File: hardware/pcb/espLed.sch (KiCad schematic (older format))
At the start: 23 parts, among them J1 led_strip, J2 flashing, J3 power, Q1 IRF9310TRPBF, Q2 AO3400A, Q3 AO3400A, Q4 AO3400A, SW1 reset, SW2 flash, U1 AMS1117-3.3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

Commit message: fix default SOT23 footprint for AO3400 mosfet
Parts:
- Q2, Q3, Q4: footprint Package_TO_SOT_SMD:SOT-23 -> custom:AO3400
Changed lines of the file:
@@
 F 0 "Q2" V 2450 4650 50  0000 L CNN
 F 1 "AO3400A" V 2375 4425 50  0000 L CNN
-F 2 "Package_TO_SOT_SMD:SOT-23" H 2375 4950 50  0001 C CNN
+F 2 "custom:AO3400" H 2375 4950 50  0001 C CNN
 F 3 "https://static.chipdip.ru/lib/046/DOC003046153.pdf" H 2175 4850 50  0001 C CNN
 	1    2175 4850
@@
 F 0 "Q3" V 3550 4650 50  0000 L CNN
 F 1 "AO3400A" V 3475 4425 50  0000 L CNN
-F 2 "Package_TO_SOT_SMD:SOT-23" H 3475 4950 50  0001 C CNN
+F 2 "custom:AO3400" H 3475 4950 50  0001 C CNN
 F 3 "https://static.chipdip.ru/lib/046/DOC003046153.pdf" H 3275 4850 50  0001 C CNN
 	1    3275 4850
@@
 F 0 "Q4" V 4650 4650 50  0000 L CNN
 F 1 "AO3400A" V 4575 4425 50  0000 L CNN
-F 2 "Package_TO_SOT_SMD:SOT-23" H 4575 4950 50  0001 C CNN
+F 2 "custom:AO3400" H 4575 4950 50  0001 C CNN
 F 3 "https://static.chipdip.ru/lib/046/DOC003046153.pdf" H 4375 4850 50  0001 C CNN
 	1    4375 4850

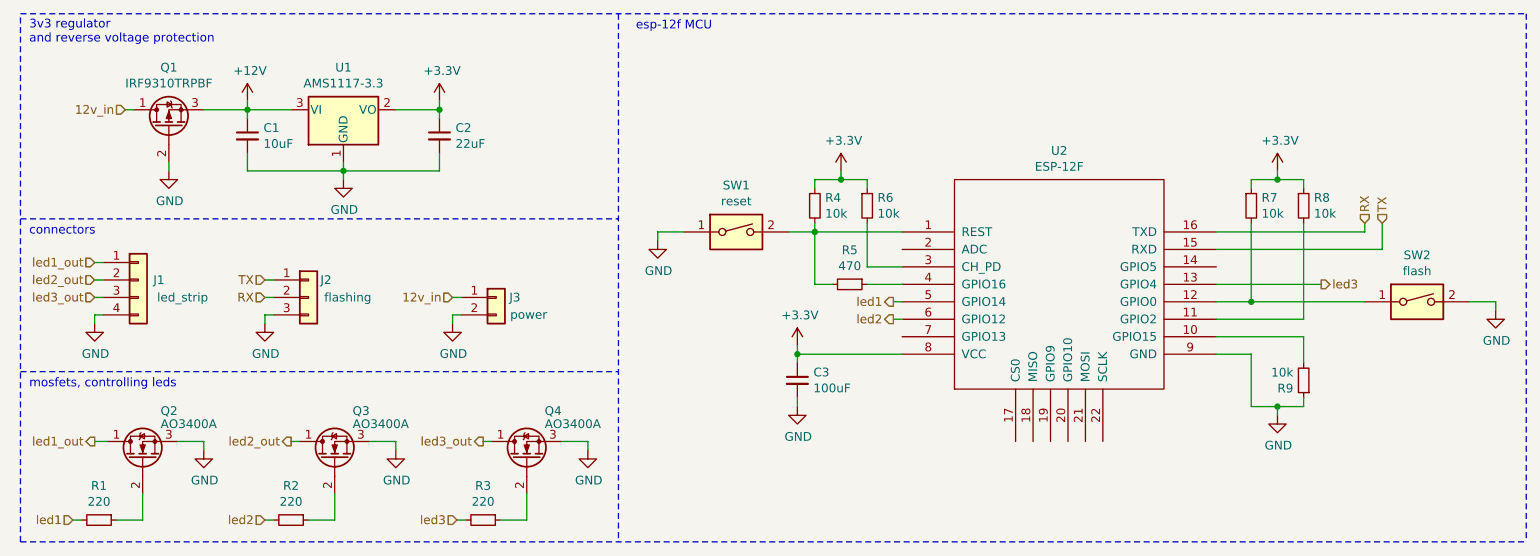
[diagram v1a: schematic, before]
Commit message: layout the 'led driver' part of the scheme
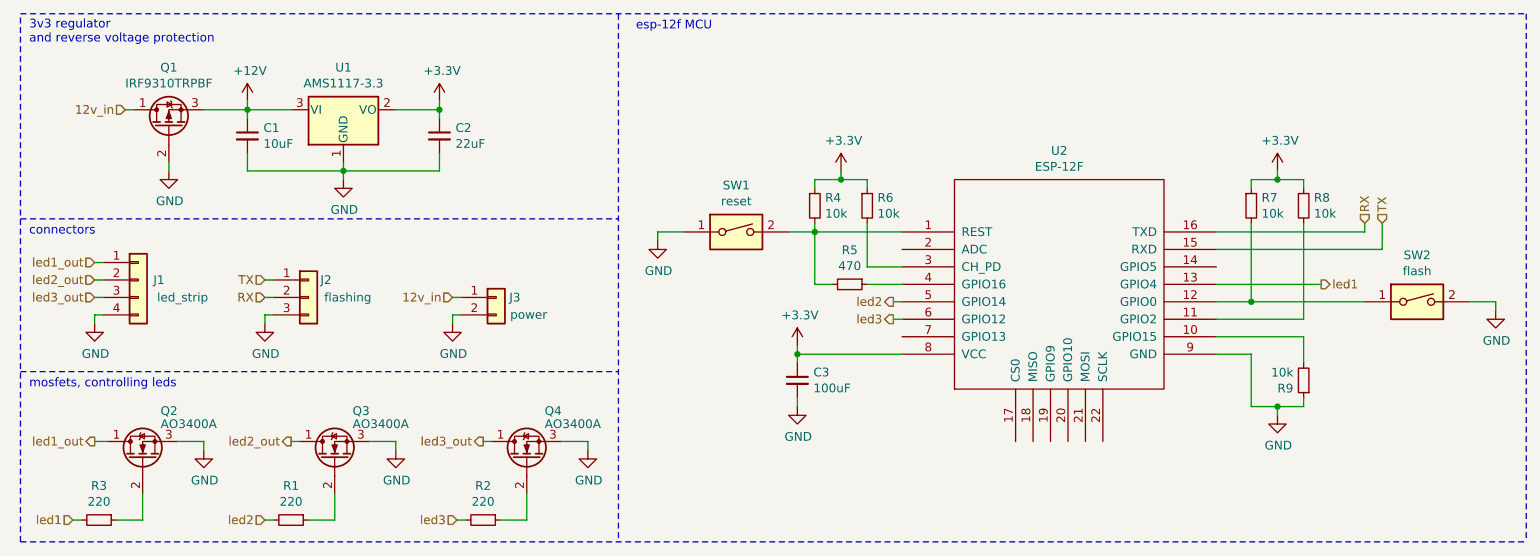
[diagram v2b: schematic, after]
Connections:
- net led1: now also R3.2, U2.13 (GPIO4); no longer R1.2, U2.5 (GPIO14)
- net led2: now also R1.2, U2.5 (GPIO14); no longer R2.2, U2.6 (GPIO12)
- net led3: now also R2.2, U2.6 (GPIO12); no longer R3.2, U2.13 (GPIO4)
- net at Q2.2 (G): now also R3.1; no longer R1.1
- net at Q3.2 (G): now also R1.1; no longer R2.1
- net at Q4.2 (G): now also R2.1; no longer R3.1
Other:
- moved on the sheet: R1, R2, R3
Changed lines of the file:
@@
 	3325 3250 3325 3200
-$Comp
-L Device:Q_PMOS_DGS Q1
-U 1 1 5FFCD3D9
-P 2325 2950
-F 0 "Q1" V 2667 2950 50  0000 C CNN
-F 1 "IRF9310TRPBF" V 2576 2950 50  0000 C CNN
-F 2 "custom:IRF9310PBF" H 2525 3050 50  0001 C CNN
-F 3 "https://static.chipdip.ru/lib/304/DOC004304962.pdf" H 2325 2950 50  0001 C CNN
-	1    2325 2950
-	0    -1   -1   0
-$EndComp
 $Comp
 L power:GND #PWR04
@@
 Wire Wire Line
 	2075 2850 2125 2850
-$Comp
-L ESP8266:ESP-12F U2
-U 1 1 5FFF27BA
-P 7425 3850
-F 0 "U2" H 7425 4615 50  0000 C CNN
-F 1 "ESP-12F" H 7425 4524 50  0000 C CNN
-F 2 "ESP8266:ESP-12E_SMD" H 7425 3850 50  0001 C CNN
-F 3 "" H 7425 3850 50  0001 C CNN
-	1    7425 3850
-	1    0    0    -1
-$EndComp
 $Comp
 L Device:R_Small R4
@@
 Wire Wire Line
 	8525 3950 9175 3950
-Text HLabel 6475 3950 0    50   Output ~ 0
-led1
 Wire Wire Line
 	6475 3950 6525 3950
 Text HLabel 9175 3500 1    50   Input ~ 0
 RX
-Text HLabel 6475 4050 0    50   Output ~ 0
-led2
 Wire Wire Line
 	6525 4050 6475 4050
-Text HLabel 8925 3850 2    50   Output ~ 0
-led3
-Wire Wire Line
-	8925 3850 8325 3850
 $Comp
 L power:GND #PWR0109
@@
 	1    0    0    -1
 $EndComp
-Text HLabel 1775 5200 0    50   Input ~ 0
-led1
-Wire Wire Line
-	1825 5200 1775 5200
+Wire Wire Line
+	2925 5200 2875 5200
 $Comp
 L Device:R_Small R1
 U 1 1 600C9AA0
-P 1925 5200
-F 0 "R1" V 1729 5200 50  0000 C CNN
-F 1 "220" V 1820 5200 50  0000 C CNN
-F 2 "Resistor_SMD:R_0805_2012Metric" H 1925 5200 50  0001 C CNN
-F 3 "~" H 1925 5200 50  0001 C CNN
-	1    1925 5200
+P 3025 5200
+F 0 "R1" V 2829 5200 50  0000 C CNN
+F 1 "220" V 2920 5200 50  0000 C CNN
+F 2 "Resistor_SMD:R_0805_2012Metric" H 3025 5200 50  0001 C CNN
+F 3 "~" H 3025 5200 50  0001 C CNN
+	1    3025 5200
 	0    1    1    0
 $EndComp
@@
 	0    -1   -1   0
 $EndComp
-Text HLabel 2875 5200 0    50   Input ~ 0
-led2
-Wire Wire Line
-	2925 5200 2875 5200
+Wire Wire Line
+	4025 5200 3975 5200
 $Comp
 L Device:R_Small R2
 U 1 1 600FDD72
-P 3025 5200
-F 0 "R2" V 2829 5200 50  0000 C CNN
-F 1 "220" V 2920 5200 50  0000 C CNN
-F 2 "Resistor_SMD:R_0805_2012Metric" H 3025 5200 50  0001 C CNN
-F 3 "~" H 3025 5200 50  0001 C CNN
-	1    3025 5200
+P 4125 5200
+F 0 "R2" V 3929 5200 50  0000 C CNN
+F 1 "220" V 4020 5200 50  0000 C CNN
+F 2 "Resistor_SMD:R_0805_2012Metric" H 4125 5200 50  0001 C CNN
+F 3 "~" H 4125 5200 50  0001 C CNN
+	1    4125 5200
 	0    1    1    0
 $EndComp
@@
 	0    -1   -1   0
 $EndComp
-Text HLabel 3975 5200 0    50   Input ~ 0
-led3
-Wire Wire Line
-	4025 5200 3975 5200
+Wire Wire Line
+	1825 5200 1775 5200
 $Comp
 L Device:R_Small R3
 U 1 1 60107E5C
-P 4125 5200
-F 0 "R3" V 3929 5200 50  0000 C CNN
-F 1 "220" V 4020 5200 50  0000 C CNN
-F 2 "Resistor_SMD:R_0805_2012Metric" H 4125 5200 50  0001 C CNN
-F 3 "~" H 4125 5200 50  0001 C CNN
-	1    4125 5200
+P 1925 5200
+F 0 "R3" V 1729 5200 50  0000 C CNN
+F 1 "220" V 1820 5200 50  0000 C CNN
+F 2 "Resistor_SMD:R_0805_2012Metric" H 1925 5200 50  0001 C CNN
+F 3 "~" H 1925 5200 50  0001 C CNN
+	1    1925 5200
 	0    1    1    0
 $EndComp
@@
 Text HLabel 1900 4750 0    50   Output ~ 0
 led1_out
-Text HLabel 3025 4750 0    50   Output ~ 0
-led2_out
 Wire Wire Line
 	3025 4750 3075 4750
@@
 Text Notes 5000 2400 0    50   ~ 0
 esp-12f MCU
+Text HLabel 6475 4050 0    50   Output ~ 0
+led3
+Wire Wire Line
+	8925 3850 8325 3850
+$Comp
+L ESP8266:ESP-12F U2
+U 1 1 5FFF27BA
+P 7425 3850
+F 0 "U2" H 7425 4615 50  0000 C CNN
+F 1 "ESP-12F" H 7425 4524 50  0000 C CNN
+F 2 "ESP8266:ESP-12E_SMD" H 7425 3850 50  0001 C CNN
+F 3 "" H 7425 3850 50  0001 C CNN
+	1    7425 3850
+	1    0    0    -1
+$EndComp
+Text HLabel 6475 3950 0    50   Output ~ 0
+led2
+Text HLabel 8925 3850 2    50   Output ~ 0
+led1
+$Comp
+L Device:Q_PMOS_DGS Q1
+U 1 1 5FFCD3D9
+P 2325 2950
+F 0 "Q1" V 2667 2950 50  0000 C CNN
+F 1 "IRF9310TRPBF" V 2576 2950 50  0000 C CNN
+F 2 "custom:IRF9310PBF" H 2525 3050 50  0001 C CNN
+F 3 "https://static.chipdip.ru/lib/304/DOC004304962.pdf" H 2325 2950 50  0001 C CNN
+	1    2325 2950
+	0    -1   -1   0
+$EndComp
+Text HLabel 3025 4750 0    50   Output ~ 0
+led2_out
+Text HLabel 3975 5200 0    50   Input ~ 0
+led3
+Text HLabel 2875 5200 0    50   Input ~ 0
+led2
+Text HLabel 1775 5200 0    50   Input ~ 0
+led1
 $EndSCHEMATC

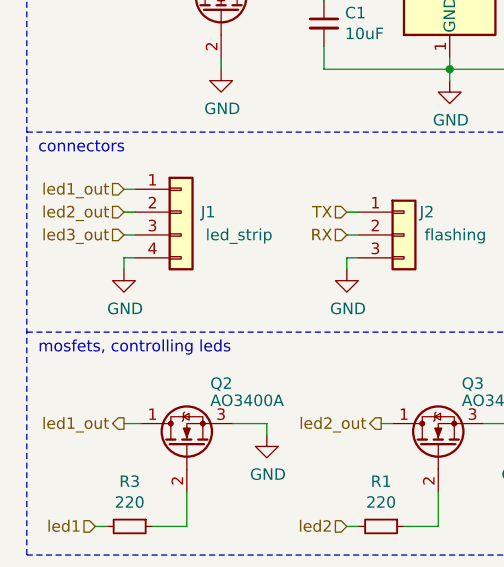
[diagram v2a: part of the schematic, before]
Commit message: replace GND with 12V in led strip connector
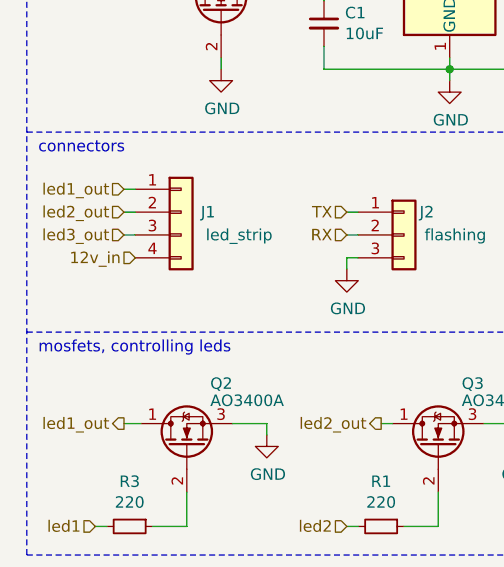
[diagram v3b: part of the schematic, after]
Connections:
- net 12v_in: now also J1.4 (Pin_4)
- net GND: no longer J1.4 (Pin_4)
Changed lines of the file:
@@
 Wire Wire Line
 	6525 4050 6475 4050
-$Comp
-L power:GND #PWR0109
-U 1 1 6009ECDE
-P 2875 4075
-F 0 "#PWR0109" H 2875 3825 50  0001 C CNN
-F 1 "GND" H 2880 3902 50  0000 C CNN
-F 2 "" H 2875 4075 50  0001 C CNN
-F 3 "" H 2875 4075 50  0001 C CNN
-	1    2875 4075
-	1    0    0    -1
-$EndComp
-Wire Wire Line
-	2875 3925 2925 3925
-Text HLabel 2875 3825 0    50   Input ~ 0
-TX
-Text HLabel 2875 3925 0    50   Input ~ 0
-RX
-$Comp
-L Connector_Generic:Conn_01x03 J2
-U 1 1 6009A6C5
-P 3125 3925
-F 0 "J2" H 3225 4025 50  0000 C CNN
-F 1 "flashing" H 3350 3925 50  0000 C CNN
-F 2 "Connector_PinSocket_2.54mm:PinSocket_1x03_P2.54mm_Vertical" H 3125 3925 50  0001 C CNN
-F 3 "~" H 3125 3925 50  0001 C CNN
-	1    3125 3925
-	1    0    0    -1
-$EndComp
 Wire Wire Line
 	2925 5200 2875 5200
@@
 Wire Wire Line
 	4125 4750 4175 4750
-Wire Wire Line
-	1900 3925 1950 3925
-Text HLabel 1900 3925 0    50   Input ~ 0
-led3_out
-Wire Wire Line
-	1900 3725 1950 3725
-Wire Wire Line
-	1900 3825 1950 3825
-Text HLabel 1900 3825 0    50   Input ~ 0
+Text Notes 1525 2475 0    50   ~ 0
+3v3 regulator\nand reverse voltage protection
+Text Notes 1525 3575 0    50   ~ 0
+connectors
+Text Notes 1525 4450 0    50   ~ 0
+mosfets, controlling leds
+Wire Notes Line
+	4900 2300 4900 5325
+Wire Notes Line
+	1475 5325 1475 2300
+Wire Notes Line
+	1475 3475 4900 3475
+Wire Notes Line
+	1475 4350 4900 4350
+Wire Notes Line
+	10100 2300 10100 5325
+Wire Notes Line
+	1475 2300 10100 2300
+Wire Notes Line
+	1475 5325 10100 5325
+Text Notes 5000 2400 0    50   ~ 0
+esp-12f MCU
+Text HLabel 6475 4050 0    50   Output ~ 0
+led3
+Wire Wire Line
+	8925 3850 8325 3850
+$Comp
+L ESP8266:ESP-12F U2
+U 1 1 5FFF27BA
+P 7425 3850
+F 0 "U2" H 7425 4615 50  0000 C CNN
+F 1 "ESP-12F" H 7425 4524 50  0000 C CNN
+F 2 "ESP8266:ESP-12E_SMD" H 7425 3850 50  0001 C CNN
+F 3 "" H 7425 3850 50  0001 C CNN
+	1    7425 3850
+	1    0    0    -1
+$EndComp
+Text HLabel 6475 3950 0    50   Output ~ 0
+led2
+Text HLabel 8925 3850 2    50   Output ~ 0
+led1
+$Comp
+L Device:Q_PMOS_DGS Q1
+U 1 1 5FFCD3D9
+P 2325 2950
+F 0 "Q1" V 2667 2950 50  0000 C CNN
+F 1 "IRF9310TRPBF" V 2576 2950 50  0000 C CNN
+F 2 "custom:IRF9310PBF" H 2525 3050 50  0001 C CNN
+F 3 "https://static.chipdip.ru/lib/304/DOC004304962.pdf" H 2325 2950 50  0001 C CNN
+	1    2325 2950
+	0    -1   -1   0
+$EndComp
+Text HLabel 3025 4750 0    50   Output ~ 0
 led2_out
-Text HLabel 1900 3725 0    50   Input ~ 0
-led1_out
-$Comp
-L power:GND #PWR0113
-U 1 1 6011AB1B
-P 1900 4075
-F 0 "#PWR0113" H 1900 3825 50  0001 C CNN
-F 1 "GND" H 1905 3902 50  0000 C CNN
-F 2 "" H 1900 4075 50  0001 C CNN
-F 3 "" H 1900 4075 50  0001 C CNN
-	1    1900 4075
-	1    0    0    -1
-$EndComp
+Text HLabel 3975 5200 0    50   Input ~ 0
+led3
+Text HLabel 2875 5200 0    50   Input ~ 0
+led2
+Text HLabel 1775 5200 0    50   Input ~ 0
+led1
+Wire Wire Line
+	3950 3925 4000 3925
+Text HLabel 3950 3925 0    50   Input ~ 0
+12v_in
+Wire Wire Line
+	3950 4025 4000 4025
+Wire Wire Line
+	3950 4075 3950 4025
+$Comp
+L power:GND #PWR0114
+U 1 1 601B52CF
+P 3950 4075
+F 0 "#PWR0114" H 3950 3825 50  0001 C CNN
+F 1 "GND" H 3955 3902 50  0000 C CNN
+F 2 "" H 3950 4075 50  0001 C CNN
+F 3 "" H 3950 4075 50  0001 C CNN
+	1    3950 4075
+	1    0    0    -1
+$EndComp
+$Comp
+L Connector_Generic:Conn_01x02 J3
+U 1 1 601B4A41
+P 4200 3925
+F 0 "J3" H 4275 3925 50  0000 L CNN
+F 1 "power" H 4280 3826 50  0000 L CNN
+F 2 "Connector_PinSocket_2.54mm:PinSocket_1x02_P2.54mm_Vertical" H 4200 3925 50  0001 C CNN
+F 3 "~" H 4200 3925 50  0001 C CNN
+	1    4200 3925
+	1    0    0    -1
+$EndComp
+Wire Wire Line
+	2875 4025 2925 4025
+Wire Wire Line
+	2875 4075 2875 4025
+Wire Wire Line
+	2875 3825 2925 3825
 $Comp
 L Connector_Generic:Conn_01x04 J1
@@
 	1    0    0    -1
 $EndComp
-Wire Wire Line
-	2875 3825 2925 3825
-Wire Wire Line
-	2875 4075 2875 4025
-Wire Wire Line
-	2875 4025 2925 4025
-Wire Wire Line
-	1900 4075 1900 4025
-Wire Wire Line
-	1900 4025 1950 4025
-$Comp
-L Connector_Generic:Conn_01x02 J3
-U 1 1 601B4A41
-P 4200 3925
-F 0 "J3" H 4275 3925 50  0000 L CNN
-F 1 "power" H 4280 3826 50  0000 L CNN
-F 2 "Connector_PinSocket_2.54mm:PinSocket_1x02_P2.54mm_Vertical" H 4200 3925 50  0001 C CNN
-F 3 "~" H 4200 3925 50  0001 C CNN
-	1    4200 3925
-	1    0    0    -1
-$EndComp
-$Comp
-L power:GND #PWR0114
-U 1 1 601B52CF
-P 3950 4075
-F 0 "#PWR0114" H 3950 3825 50  0001 C CNN
-F 1 "GND" H 3955 3902 50  0000 C CNN
-F 2 "" H 3950 4075 50  0001 C CNN
-F 3 "" H 3950 4075 50  0001 C CNN
-	1    3950 4075
-	1    0    0    -1
-$EndComp
-Wire Wire Line
-	3950 4075 3950 4025
-Wire Wire Line
-	3950 4025 4000 4025
-Text HLabel 3950 3925 0    50   Input ~ 0
+Text HLabel 1900 3725 0    50   Input ~ 0
+led1_out
+Text HLabel 1900 3825 0    50   Input ~ 0
+led2_out
+Wire Wire Line
+	1900 3825 1950 3825
+Wire Wire Line
+	1900 3725 1950 3725
+Text HLabel 1900 3925 0    50   Input ~ 0
+led3_out
+Wire Wire Line
+	1900 3925 1950 3925
+$Comp
+L Connector_Generic:Conn_01x03 J2
+U 1 1 6009A6C5
+P 3125 3925
+F 0 "J2" H 3225 4025 50  0000 C CNN
+F 1 "flashing" H 3350 3925 50  0000 C CNN
+F 2 "Connector_PinSocket_2.54mm:PinSocket_1x03_P2.54mm_Vertical" H 3125 3925 50  0001 C CNN
+F 3 "~" H 3125 3925 50  0001 C CNN
+	1    3125 3925
+	1    0    0    -1
+$EndComp
+Text HLabel 2875 3925 0    50   Input ~ 0
+RX
+Text HLabel 2875 3825 0    50   Input ~ 0
+TX
+Wire Wire Line
+	2875 3925 2925 3925
+$Comp
+L power:GND #PWR0109
+U 1 1 6009ECDE
+P 2875 4075
+F 0 "#PWR0109" H 2875 3825 50  0001 C CNN
+F 1 "GND" H 2880 3902 50  0000 C CNN
+F 2 "" H 2875 4075 50  0001 C CNN
+F 3 "" H 2875 4075 50  0001 C CNN
+	1    2875 4075
+	1    0    0    -1
+$EndComp
+Text HLabel 1950 4025 0    50   Input ~ 0
 12v_in
-Wire Wire Line
-	3950 3925 4000 3925
-Text Notes 1525 2475 0    50   ~ 0
-3v3 regulator\nand reverse voltage protection
-Text Notes 1525 3575 0    50   ~ 0
-connectors
-Text Notes 1525 4450 0    50   ~ 0
-mosfets, controlling leds
-Wire Notes Line
-	4900 2300 4900 5325
-Wire Notes Line
-	1475 5325 1475 2300
-Wire Notes Line
-	1475 3475 4900 3475
-Wire Notes Line
-	1475 4350 4900 4350
-Wire Notes Line
-	10100 2300 10100 5325
-Wire Notes Line
-	1475 2300 10100 2300
-Wire Notes Line
-	1475 5325 10100 5325
-Text Notes 5000 2400 0    50   ~ 0
-esp-12f MCU
-Text HLabel 6475 4050 0    50   Output ~ 0
-led3
-Wire Wire Line
-	8925 3850 8325 3850
-$Comp
-L ESP8266:ESP-12F U2
-U 1 1 5FFF27BA
-P 7425 3850
-F 0 "U2" H 7425 4615 50  0000 C CNN
-F 1 "ESP-12F" H 7425 4524 50  0000 C CNN
-F 2 "ESP8266:ESP-12E_SMD" H 7425 3850 50  0001 C CNN
-F 3 "" H 7425 3850 50  0001 C CNN
-	1    7425 3850
-	1    0    0    -1
-$EndComp
-Text HLabel 6475 3950 0    50   Output ~ 0
-led2
-Text HLabel 8925 3850 2    50   Output ~ 0
-led1
-$Comp
-L Device:Q_PMOS_DGS Q1
-U 1 1 5FFCD3D9
-P 2325 2950
-F 0 "Q1" V 2667 2950 50  0000 C CNN
-F 1 "IRF9310TRPBF" V 2576 2950 50  0000 C CNN
-F 2 "custom:IRF9310PBF" H 2525 3050 50  0001 C CNN
-F 3 "https://static.chipdip.ru/lib/304/DOC004304962.pdf" H 2325 2950 50  0001 C CNN
-	1    2325 2950
-	0    -1   -1   0
-$EndComp
-Text HLabel 3025 4750 0    50   Output ~ 0
-led2_out
-Text HLabel 3975 5200 0    50   Input ~ 0
-led3
-Text HLabel 2875 5200 0    50   Input ~ 0
-led2
-Text HLabel 1775 5200 0    50   Input ~ 0
-led1
 $EndSCHEMATC
